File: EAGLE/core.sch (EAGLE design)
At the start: 47 parts, among them Q1 MMDT3904, U1 MIC5219, U3 STM32F10XCXT6, U4 SST25VF040B-50-4I-S2AF, X1 USB-MICROB, Y1 8Mhz

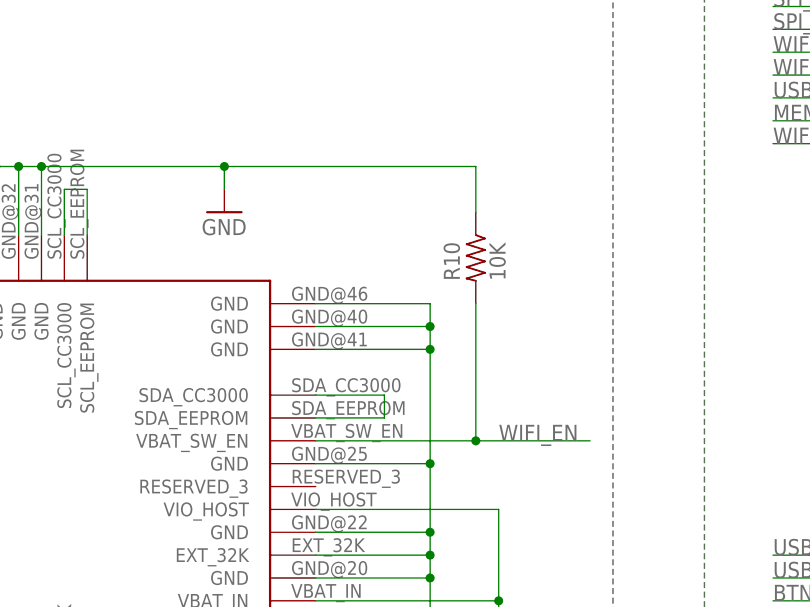
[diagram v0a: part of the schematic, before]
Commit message: Better USB, improved power layout, got rid of resistor near antenna
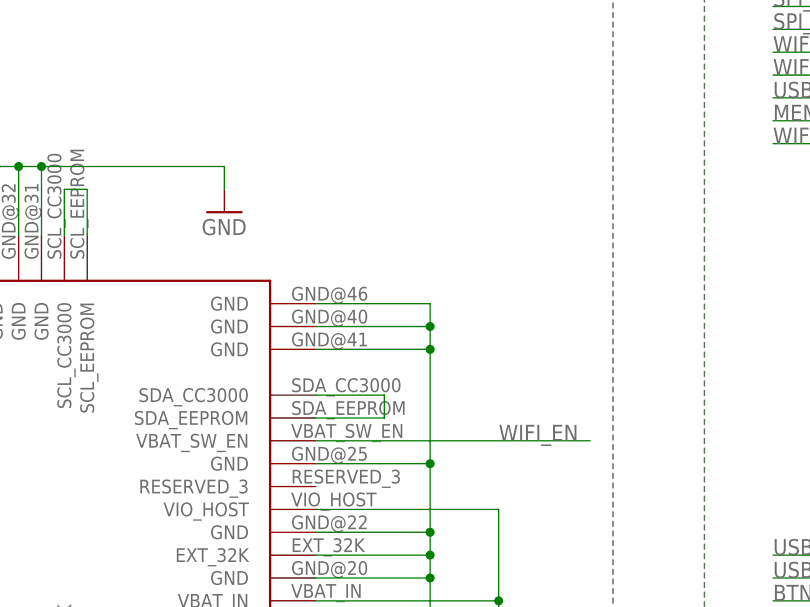
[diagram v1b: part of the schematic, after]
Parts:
- removed R10: 10K, rcl:R-US_R0603
- X1: value USB-MICROB -> USBUSB-MICROB-ALIGN; device SparkFun-Connectors:USB-MICROB -> Spark:USBUSB-MICROB-ALIGN
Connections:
- net GND: no longer R10.1
- net WIFI_EN: no longer R10.2
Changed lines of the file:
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@@
 <part name="R5" library="rcl" deviceset="R-US_" device="R0603" value="22"/>
 <part name="R6" library="rcl" deviceset="R-US_" device="R0603" value="22"/>
-<part name="X1" library="SparkFun-Connectors" deviceset="USB" device="-MICROB"/>
+<part name="X1" library="Spark" deviceset="USB" device="USB-MICROB-ALIGN"/>
 <part name="GND3" library="SparkFun" deviceset="GND" device=""/>
 <part name="F1" library="SparkFun" deviceset="PTC" device="SMD" value="500mA"/>
@@
 <part name="C5" library="rcl" deviceset="C-EU" device="C0603" value="100nF"/>
 <part name="R9" library="rcl" deviceset="R-US_" device="R0603" value="10K"/>
-<part name="R10" library="rcl" deviceset="R-US_" device="R0603" value="10K"/>
 <part name="Q1" library="SparkFun-DiscreteSemi" deviceset="MMDT3904" device=""/>
 <part name="R14" library="rcl" deviceset="R-US_" device="R0603" value="1K"/>
@@
 <attribute name="VALUE" x="158.75" y="61.468" size="1.778" layer="96"/>
 </instance>
-<instance part="R10" gate="G$1" x="231.14" y="144.78" smashed="yes" rot="R270">
-<attribute name="NAME" x="229.362" y="142.24" size="1.778" layer="95" rot="R90"/>
-<attribute name="VALUE" x="234.442" y="142.24" size="1.778" layer="96" rot="R90"/>
-</instance>
 <instance part="Q1" gate="G$1" x="52.07" y="64.77" smashed="yes" rot="R90">
 <attribute name="NAME" x="48.26" y="68.58" size="1.778" layer="95"/>
@@
 <wire x1="170.18" y1="154.94" x2="170.18" y2="147.32" width="0.1524" layer="91"/>
 <junction x="175.26" y="154.94"/>
-<pinref part="R10" gate="G$1" pin="1"/>
-<wire x1="231.14" y1="149.86" x2="231.14" y2="154.94" width="0.1524" layer="91"/>
-<wire x1="231.14" y1="154.94" x2="203.2" y2="154.94" width="0.1524" layer="91"/>
-<junction x="203.2" y="154.94"/>
 </segment>
 <segment>
@@
 <segment>
 <pinref part="U2" gate="G$1" pin="VBAT_SW_EN"/>
-<wire x1="213.36" y1="124.46" x2="231.14" y2="124.46" width="0.1524" layer="91"/>
+<wire x1="213.36" y1="124.46" x2="243.84" y2="124.46" width="0.1524" layer="91"/>
 <label x="233.68" y="124.46" size="1.778" layer="95"/>
-<pinref part="R10" gate="G$1" pin="2"/>
-<wire x1="231.14" y1="124.46" x2="231.14" y2="139.7" width="0.1524" layer="91"/>
-<wire x1="231.14" y1="124.46" x2="243.84" y2="124.46" width="0.1524" layer="91"/>
-<junction x="231.14" y="124.46"/>
-</segment>
-<segment>
+</segment>
+<segment>

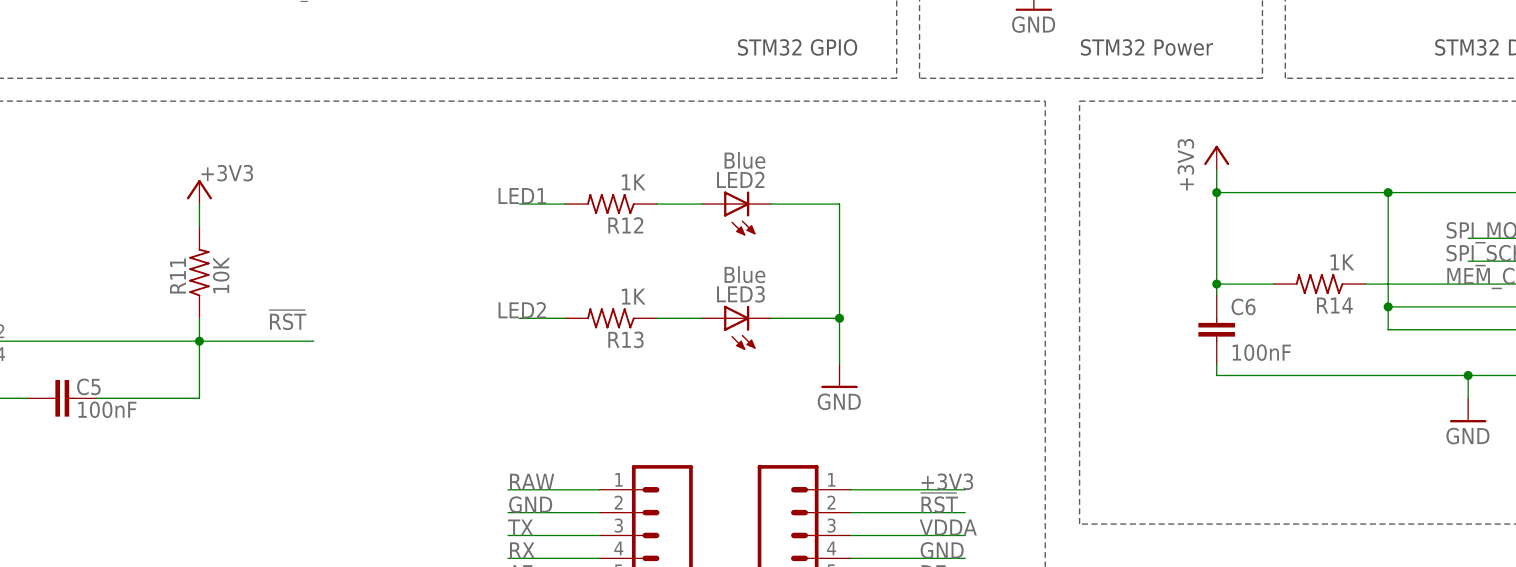
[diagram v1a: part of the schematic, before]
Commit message: Renumbered parts
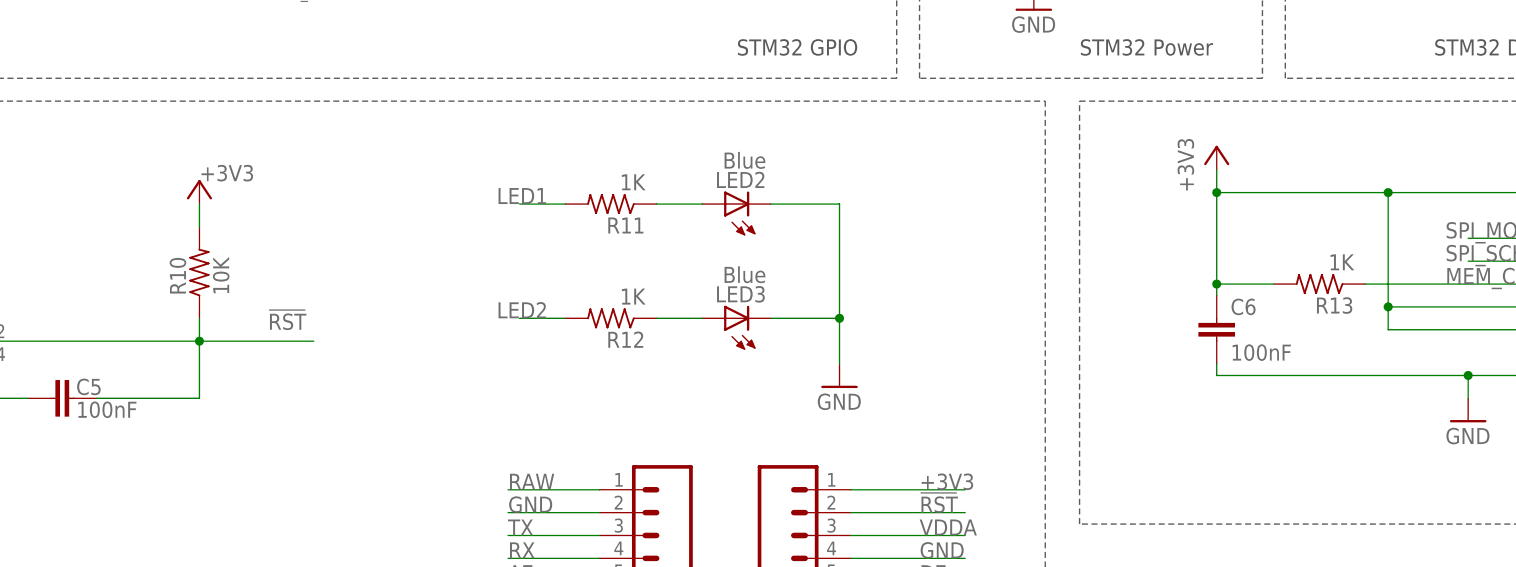
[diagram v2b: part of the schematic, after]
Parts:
- removed R14: 1K, rcl:R-US_R0603
- added R10: 10K, rcl:R-US_R0603
- R11: value 10K -> 1K
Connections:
- net !RST: now also R10.1; no longer R11.1
- net +3V3: now also R10.2, R13.2; no longer R11.2, R14.2
- net LED1: now also R11.2; no longer R12.2
- net LED2: now also R12.2; no longer R13.2
- net MEM_CS: now also R13.1; no longer R14.1
- net N$10: now also R12.1; no longer R13.1
- net N$2: now also R11.1; no longer R12.1
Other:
- moved on the sheet: R11, R12, R13
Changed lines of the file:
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@@
 <part name="C3" library="rcl" deviceset="C-EU" device="C0603" value="100nF"/>
 <part name="RESET" library="okie" deviceset="BUTTON-KMR241GLFS" device="" value="KMR211GLFS"/>
-<part name="R11" library="rcl" deviceset="R-US_" device="R0603" value="10K"/>
+<part name="R10" library="rcl" deviceset="R-US_" device="R0603" value="10K"/>
 <part name="BTN" library="okie" deviceset="BUTTON-KMR241GLFS" device="" value="KMR211GLFS"/>
-<part name="R13" library="rcl" deviceset="R-US_" device="R0603" value="1K"/>
+<part name="R12" library="rcl" deviceset="R-US_" device="R0603" value="1K"/>
 <part name="LED3" library="SparkFun" deviceset="LED" device="0603" value="Blue"/>
 <part name="GND1" library="SparkFun" deviceset="GND" device=""/>
 <part name="LED2" library="SparkFun" deviceset="LED" device="0603" value="Blue"/>
-<part name="R12" library="rcl" deviceset="R-US_" device="R0603" value="1K"/>
+<part name="R11" library="rcl" deviceset="R-US_" device="R0603" value="1K"/>
 <part name="GND12" library="SparkFun" deviceset="GND" device=""/>
 <part name="+3V2" library="supply1" deviceset="+3V3" device=""/>
@@
 <part name="R9" library="rcl" deviceset="R-US_" device="R0603" value="10K"/>
 <part name="Q1" library="SparkFun-DiscreteSemi" deviceset="MMDT3904" device=""/>
-<part name="R14" library="rcl" deviceset="R-US_" device="R0603" value="1K"/>
+<part name="R13" library="rcl" deviceset="R-US_" device="R0603" value="1K"/>
 <part name="C6" library="rcl" deviceset="C-EU" device="C0603" value="100nF"/>
 <part name="VDDA" library="supply2" deviceset="VCC" device=""/>
@@
 <attribute name="NAME" x="273.05" y="64.77" size="1.778" layer="95"/>
 </instance>
-<instance part="R11" gate="G$1" x="303.53" y="67.31" smashed="yes" rot="R90">
+<instance part="R10" gate="G$1" x="303.53" y="67.31" smashed="yes" rot="R90">
 <attribute name="NAME" x="302.0314" y="64.77" size="1.778" layer="95" rot="R90"/>
 <attribute name="VALUE" x="306.832" y="64.77" size="1.778" layer="96" rot="R90"/>
@@
 <attribute name="NAME" x="288.29" y="26.67" size="1.778" layer="95"/>
 </instance>
-<instance part="R13" gate="G$1" x="349.25" y="62.23" rot="R180"/>
+<instance part="R12" gate="G$1" x="349.25" y="62.23" rot="R180"/>
 <instance part="LED3" gate="G$1" x="361.95" y="62.23" rot="R90"/>
 <instance part="GND1" gate="1" x="374.65" y="54.61"/>
 <instance part="LED2" gate="G$1" x="361.95" y="74.93" rot="R90"/>
-<instance part="R12" gate="G$1" x="349.25" y="74.93" rot="R180"/>
+<instance part="R11" gate="G$1" x="349.25" y="74.93" rot="R180"/>
 <instance part="GND12" gate="1" x="267.97" y="39.37"/>
 <instance part="+3V2" gate="G$1" x="303.53" y="77.47" smashed="yes">
@@
 <attribute name="NAME" x="62.23" y="44.45" size="1.778" layer="95" rot="R180"/>
 </instance>
-<instance part="R14" gate="G$1" x="427.99" y="66.04" rot="R180"/>
+<instance part="R13" gate="G$1" x="427.99" y="66.04" rot="R180"/>
 <instance part="C6" gate="G$1" x="416.56" y="62.23" smashed="yes">
 <attribute name="NAME" x="418.084" y="62.611" size="1.778" layer="95"/>
@@
 <segment>
 <wire x1="303.53" y1="72.39" x2="303.53" y2="74.93" width="0.1524" layer="91"/>
-<pinref part="R11" gate="G$1" pin="2"/>
+<pinref part="R10" gate="G$1" pin="2"/>
 <pinref part="+3V2" gate="G$1" pin="+3V3"/>
 </segment>
@@
 <wire x1="435.61" y1="76.2" x2="416.56" y2="76.2" width="0.1524" layer="91"/>
 <wire x1="416.56" y1="78.74" x2="416.56" y2="76.2" width="0.1524" layer="91"/>
-<pinref part="R14" gate="G$1" pin="2"/>
+<pinref part="R13" gate="G$1" pin="2"/>
 <wire x1="422.91" y1="66.04" x2="416.56" y2="66.04" width="0.1524" layer="91"/>
 <wire x1="416.56" y1="66.04" x2="416.56" y2="76.2" width="0.1524" layer="91"/>
@@
 <label x="311.15" y="60.96" size="1.778" layer="95"/>
 <pinref part="RESET" gate="G$1" pin="2"/>
-<pinref part="R11" gate="G$1" pin="1"/>
+<pinref part="R10" gate="G$1" pin="1"/>
 <pinref part="C5" gate="G$1" pin="2"/>
 <wire x1="292.1" y1="53.34" x2="303.53" y2="53.34" width="0.1524" layer="91"/>
@@
 <net name="N$2" class="0">
 <segment>
-<pinref part="R12" gate="G$1" pin="1"/>
+<pinref part="R11" gate="G$1" pin="1"/>
 <pinref part="LED2" gate="G$1" pin="A"/>
 <wire x1="354.33" y1="74.93" x2="359.41" y2="74.93" width="0.1524" layer="91"/>
@@
 <net name="N$10" class="0">
 <segment>
-<pinref part="R13" gate="G$1" pin="1"/>
+<pinref part="R12" gate="G$1" pin="1"/>
 <pinref part="LED3" gate="G$1" pin="A"/>
 <wire x1="354.33" y1="62.23" x2="359.41" y2="62.23" width="0.1524" layer="91"/>
@@
 <wire x1="457.2" y1="66.04" x2="433.07" y2="66.04" width="0.1524" layer="91"/>
 <label x="441.96" y="66.04" size="1.778" layer="95"/>
-<pinref part="R14" gate="G$1" pin="1"/>
+<pinref part="R13" gate="G$1" pin="1"/>
 </segment>
 <segment>
@@
 </segment>
 <segment>
-<pinref part="R12" gate="G$1" pin="2"/>
+<pinref part="R11" gate="G$1" pin="2"/>
 <wire x1="344.17" y1="74.93" x2="339.09" y2="74.93" width="0.1524" layer="91"/>
 <label x="336.55" y="74.93" size="1.778" layer="95"/>
@@
 </segment>
 <segment>
-<pinref part="R13" gate="G$1" pin="2"/>
+<pinref part="R12" gate="G$1" pin="2"/>
 <wire x1="344.17" y1="62.23" x2="339.09" y2="62.23" width="0.1524" layer="91"/>
 <label x="336.55" y="62.23" size="1.778" layer="95"/>

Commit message: Updated assembly sheets to v0.1.0
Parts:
- X1: value USBUSB-MICROB-ALIGN -> USB-MICROB
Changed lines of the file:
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@@
 <part name="R5" library="rcl" deviceset="R-US_" device="R0603" value="22"/>
 <part name="R6" library="rcl" deviceset="R-US_" device="R0603" value="22"/>
-<part name="X1" library="Spark" deviceset="USB" device="USB-MICROB-ALIGN"/>
+<part name="X1" library="Spark" deviceset="USB" device="USB-MICROB-ALIGN" value="USB-MICROB"/>
 <part name="GND3" library="SparkFun" deviceset="GND" device=""/>
 <part name="F1" library="SparkFun" deviceset="PTC" device="SMD" value="500mA"/>

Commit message: WIP for Issue #5, #7, #8, #9
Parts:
- removed LED1: Red, SparkFun:LED0603
- removed R8: 1K, rcl:R-US_R0603
- added C14, C15: 12.5pF, rcl:C-EUC0603
- added Y2: 32Khz, Spark:Q_FC135
- U4: value SST25VF040B-50-4I-S2AF -> SST25VF040B-Q; device Silicon_Storage_Tech_By_element14_Batch_1:SST25VF040B-50-4I-S2AF -> Spark:SST25VF040B-Q
- Y1: device SparkFun:CRYSTAL5X3 -> Spark:Q_3.2X2.5
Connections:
- net OSC1 renamed OSC_OUT
- net OSC2 renamed OSC_IN
- removed net N$38: LED1.A, R8.1
- new net OSC32_IN: C15.1, U3PORTC.PC14, Y2.1
- new net OSC32_OUT: C14.1, U3PORTC.PC15, Y2.2
- net +3V3: no longer R8.2
- net GND: now also C14.2, C15.2; no longer LED1.C
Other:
- moved on the sheet: C10, C11, C7, C8, C9

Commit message: Schematic completed as per latest issues list (Ready for review)
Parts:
- removed A1: ANTENNA2SMD5, SparkFun-RF:ANTENNA2SMD5
- removed F1: 500mA, SparkFun:PTCSMD
- removed LED2, LED3: Blue, SparkFun:LED0603
- removed R11, R12: 1K, rcl:R-US_R0603
- removed R9: 10K, rcl:R-US_R0603
- removed U1: MIC5219, SparkFun:V_REG_LDOSMD
- added ANT1: AT8010, Spark:AT8010
- added C16: 10pF, rcl:C-EUC0603
- added IC1: MCP1825S-3302E, Spark:MCP1825S-SOT223
- added LED_RGB: (no value), Spark:TOPLED-3PLCC
- added LED_USR: (no value), SparkFun:LED0603
- added RN1: EXB-38V102JV, resistor-dil:4R-NEXB38V
- added X2: IPEX-20279-001E, Spark:IPEX-20279-001E
- C1: value 10uF -> 4.7uF; device SparkFun:CAP_POL1206 -> rcl:C-EUC0603
- C2: value 10uF -> 1uF; device SparkFun:CAP_POL1206 -> rcl:C-EUC0603
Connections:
- removed net N$10: LED3.A, R12.1
- removed net N$5: A1.SIGNAL, C4.1
- new net LED3: RN1B.2, U3PORTA_H.PA9
- new net LED4: RN1A.2, U3PORTA_H.PA10
- new net N$14: LED_RGB.CGREEN, RN1A.1
- new net N$17: LED_RGB.CBLUE, RN1B.1
- new net N$18: LED_RGB.CRED, RN1C.1
- net +3V3: now also C2.1, IC1.OUT, LED_RGB.A2; no longer C2.+, R9.2, U1.OUT
- net BTN: now also U3PORTB_L.PB2; no longer U3PORTA_H.PA10
- net D7: now also RN1D.1
- net GND: now also C1.2, C2.2, IC1.GND@1, IC1.GND@2, LED_USR.C, X2.GND@1; no longer C1.-, C2.-, LED2.C, LED3.C, U1.GND
- net LED1: now also LED_USR.A, RN1D.2; no longer R11.2, U3PORTA_H.PA8
- net LED2: now also RN1C.2, U3PORTA_H.PA8; no longer R12.2, U3PORTA_H.PA9
- net N$2: now also C16.2, X2.1; no longer LED2.A, R11.1
- net N$3: now also ANT1.SIGNAL, C4.1; no longer D1.A, F1.2
- net N$4: now also C16.1
- net RAW: now also C1.1, IC1.IN; no longer C1.+, U1.EN, U1.IN
- net UVCC: now also D1.A; no longer F1.1
- net WIFI_CS: no longer R9.1
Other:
- note added: "Max Voltage Input: 6VDC"
- note added: "VCC = 3.3V Output"
- note removed: "Max Voltage Input: 16VDC"
- note removed: "VCC = 5V or 3.3V Output"
- moved on the sheet: BTN, C14, C15, C5, C8, C9, D1, JP1, JP2, L1, R10, RESET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
